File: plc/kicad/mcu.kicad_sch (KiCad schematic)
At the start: 66 parts, among them J1 Conn_01x03_Pin, J2 Conn_01x04_Pin, Q3 L8050QLT1G, Q4 L8050QLT1G, SW1 TSD003B08026A03, SW2 TSD003B08026A03, U10 ESP32-S3-MINI-1U, U11 BS-0601-SK-4W, U12 AHT20_C2757850, U13 CP2102N-A02-GQFN28R, U9 RV-3028-C7

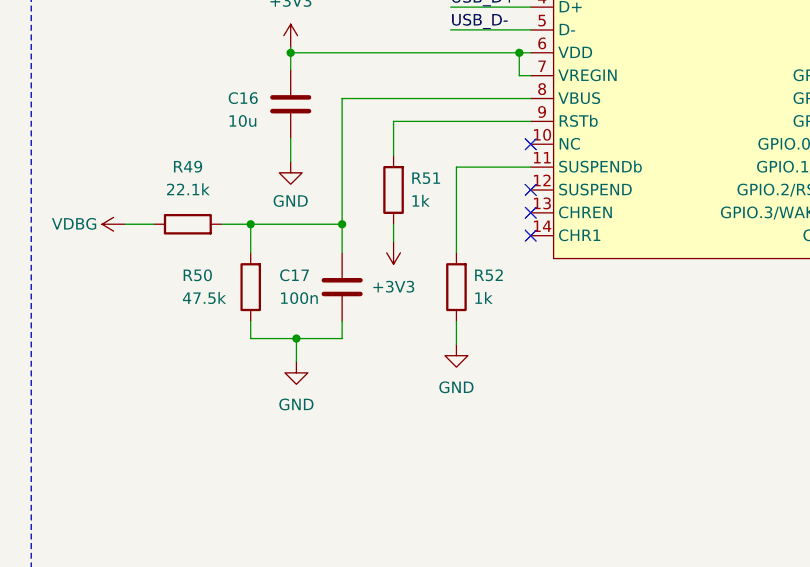
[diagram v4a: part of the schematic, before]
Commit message: PCB placement of USB circuits
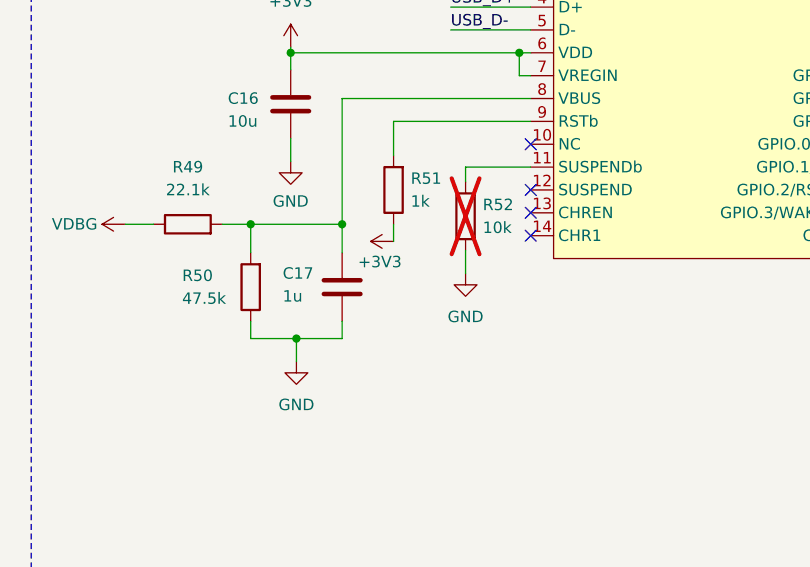
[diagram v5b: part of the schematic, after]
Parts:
- C17: value 100n -> 1u
- R52: value 1k -> 10k; now not fitted; now left out of the parts list
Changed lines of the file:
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@@
 	(wire
 		(pts
-			(xy 278.384 73.914) (xy 270.129 73.914)
+			(xy 278.384 73.914) (xy 271.145 73.914)
 		)
 		(stroke
@@
 	(wire
 		(pts
-			(xy 270.129 93.599) (xy 270.129 91.059)
+			(xy 271.145 85.725) (xy 271.145 83.185)
 		)
 		(stroke
@@
 	(wire
 		(pts
-			(xy 270.129 73.914) (xy 270.129 83.439)
+			(xy 271.145 73.914) (xy 271.145 75.565)
 		)
 		(stroke
@@
 		(dnp no)
 		(property "Reference" "C17"
-			(at 250.444 85.979 0)
+			(at 250.825 85.725 0)
 			(show_name no)
 			(do_not_autoplace no)
@@
 			)
 		)
-		(property "Value" "100n"
-			(at 250.444 88.519 0)
+		(property "Value" "1u"
+			(at 250.825 88.265 0)
 			(show_name no)
 			(do_not_autoplace no)
@@
 	(symbol
 		(lib_id "Device:R")
-		(at 270.129 87.249 180)
+		(at 271.145 79.375 180)
 		(unit 1)
 		(body_style 1)
 		(exclude_from_sim no)
-		(in_bom yes)
-		(on_board yes)
-		(in_pos_files yes)
-		(dnp no)
+		(in_bom no)
+		(on_board no)
+		(in_pos_files no)
+		(dnp yes)
 		(fields_autoplaced yes)
 		(property "Reference" "R52"
-			(at 272.034 85.9789 0)
+			(at 273.05 78.1049 0)
 			(show_name no)
 			(do_not_autoplace no)
@@
 			)
 		)
-		(property "Value" "1k"
-			(at 272.034 88.5189 0)
+		(property "Value" "10k"
+			(at 273.05 80.6449 0)
 			(show_name no)
 			(do_not_autoplace no)
@@
 		)
 		(property "Footprint" "Resistor_SMD:R_0603_1608Metric"
-			(at 271.907 87.249 90)
+			(at 272.923 79.375 90)
 			(hide yes)
 			(show_name no)
@@
 		)
 		(property "Datasheet" ""
-			(at 270.129 87.249 0)
+			(at 271.145 79.375 0)
 			(hide yes)
 			(show_name no)
@@
 		)
 		(property "Description" "Resistor"
-			(at 270.129 87.249 0)
+			(at 271.145 79.375 0)
 			(hide yes)
 			(show_name no)
@@
 	(symbol
 		(lib_id "power:GND")
-		(at 270.129 93.599 0)
+		(at 271.145 85.725 0)
 		(unit 1)
 		(body_style 1)
@@
 		(fields_autoplaced yes)
 		(property "Reference" "#PWR0109"
-			(at 270.129 99.949 0)
+			(at 271.145 92.075 0)
 			(hide yes)
 			(show_name no)
@@
 		)
 		(property "Value" "GND"
-			(at 270.129 98.425 0)
+			(at 271.145 90.551 0)
 			(show_name no)
 			(do_not_autoplace no)
@@
 		)
 		(property "Footprint" ""
-			(at 270.129 93.599 0)
+			(at 271.145 85.725 0)
 			(hide yes)
 			(show_name no)
@@
 		)
 		(property "Datasheet" ""
-			(at 270.129 93.599 0)
+			(at 271.145 85.725 0)
 			(hide yes)
 			(show_name no)
@@
 		)
 		(property "Description" "Power symbol creates a global label with name \"GND\" , ground"
-			(at 270.129 93.599 0)
+			(at 271.145 85.725 0)
 			(hide yes)
 			(show_name no)
@@
 	(symbol
 		(lib_id "power:+3V3")
-		(at 263.144 82.169 180)
+		(at 263.144 82.169 90)
 		(unit 1)
 		(body_style 1)
@@
 		(in_pos_files yes)
 		(dnp no)
-		(fields_autoplaced yes)
 		(property "Reference" "#PWR0107"
-			(at 263.144 78.359 0)
+			(at 266.954 82.169 0)
 			(hide yes)
 			(show_name no)
@@
 		)
 		(property "Value" "+3V3"
-			(at 263.144 87.249 0)
+			(at 261.62 84.455 90)
 			(show_name no)
 			(do_not_autoplace no)

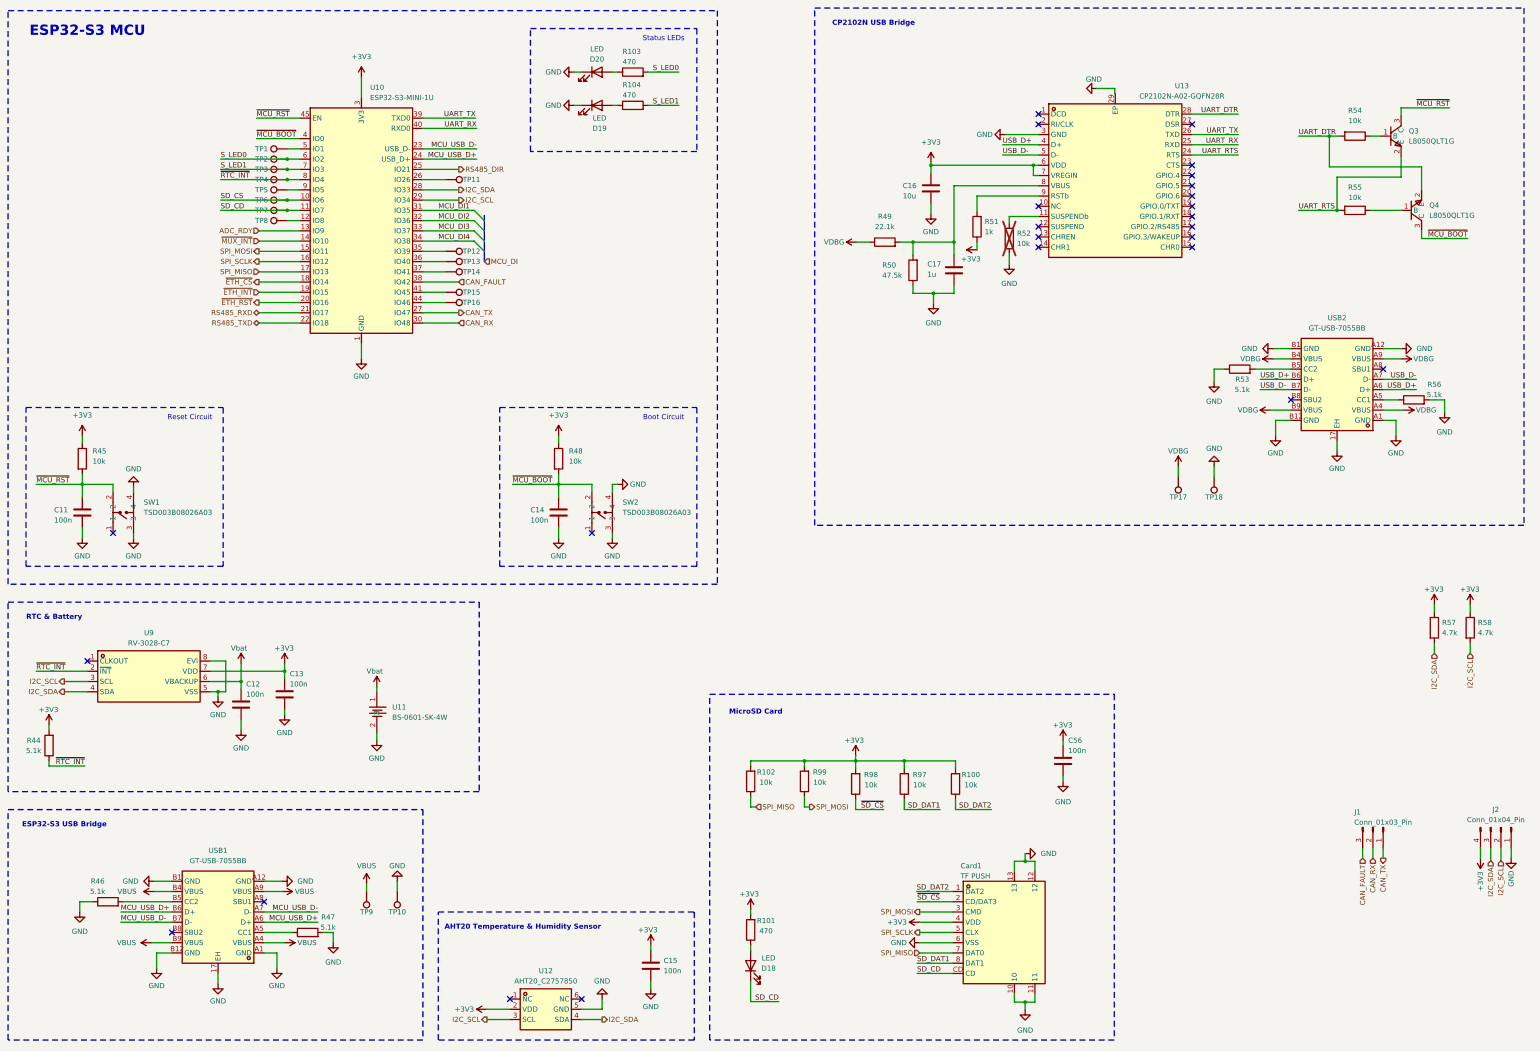
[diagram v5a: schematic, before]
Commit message: Rearranged small PCB placements
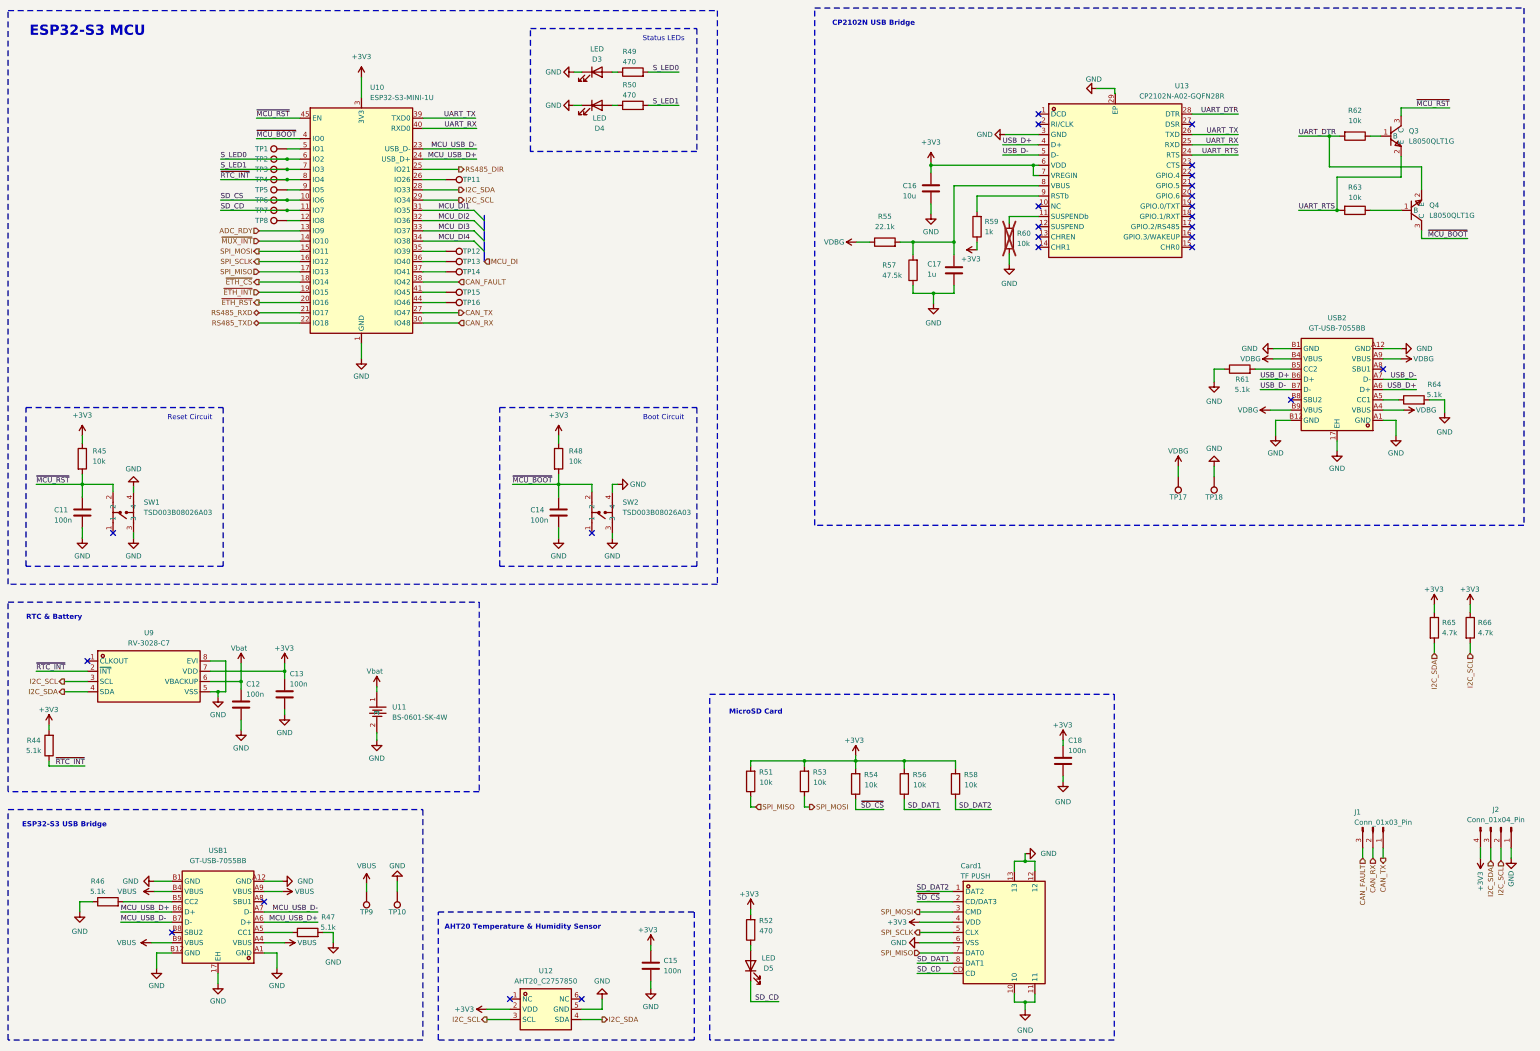
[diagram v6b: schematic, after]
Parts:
- renumbered C56 to C18, D20 to D3, D19 to D4, D18 to D5, R103 to R49, R104 to R50, R102 to R51, R101 to R52, R99 to R53, R98 to R54, R49 to R55, R97 to R56, R50 to R57, R100 to R58, R51 to R59, R52 to R60, R53 to R61, R54 to R62, R55 to R63, R56 to R64, R57 to R65, R58 to R66

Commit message: PCB placement updates
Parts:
- U10: footprint RF_Module:ESP32-S2-MINI-1U -> LibrePLC32:BULETM-SMD_ESPRESSIF_ESP32-S3-MINI-1U-N8
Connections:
- net ~{MCU_RST}: no longer U10.45 (EN)
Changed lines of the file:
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@@
 	(wire
 		(pts
-			(xy 134.62 97.79) (xy 125.73 97.79)
+			(xy 125.73 52.07) (xy 139.065 52.07)
 		)
 		(stroke
@@
 	(wire
 		(pts
-			(xy 84.455 49.53) (xy 95.25 49.53)
+			(xy 134.62 97.79) (xy 125.73 97.79)
 		)
 		(stroke
@@
 	(wire
 		(pts
-			(xy 125.73 49.53) (xy 138.811 49.53)
-		)
-		(stroke
-			(width 0)
-			(type default)
-		)
-	)
-	(wire
-		(pts
 			(xy 59.69 260.35) (xy 59.69 256.54)
 		)
@@
 	(wire
 		(pts
+			(xy 139.065 59.69) (xy 125.73 59.69)
+		)
+		(stroke
+			(width 0)
+			(type default)
+		)
+	)
+	(wire
+		(pts
+			(xy 139.065 57.15) (xy 125.73 57.15)
+		)
+		(stroke
+			(width 0)
+			(type default)
+		)
+	)
+	(wire
+		(pts
 			(xy 248.285 259.08) (xy 257.175 259.08)
 		)
@@
 	(wire
 		(pts
-			(xy 125.73 59.69) (xy 139.065 59.69)
-		)
-		(stroke
-			(width 0)
-			(type default)
-		)
-	)
-	(wire
-		(pts
 			(xy 29.845 186.69) (xy 42.545 186.69)
 		)
@@
 	(wire
 		(pts
-			(xy 125.73 52.07) (xy 139.065 52.07)
-		)
-		(stroke
-			(width 0)
-			(type default)
-		)
-	)
-	(wire
-		(pts
 			(xy 278.384 61.214) (xy 277.114 61.214)
 		)
@@
 	(wire
 		(pts
+			(xy 125.73 49.53) (xy 138.811 49.53)
+		)
+		(stroke
+			(width 0)
+			(type default)
+		)
+	)
+	(wire
+		(pts
 			(xy 131.445 64.77) (xy 125.73 64.77)
 		)
@@
 	(wire
 		(pts
-			(xy 125.73 57.15) (xy 139.065 57.15)
-		)
-		(stroke
-			(width 0)
-			(type default)
-		)
-	)
-	(wire
-		(pts
 			(xy 372.11 116.84) (xy 363.855 116.84)
 		)
@@
 		)
 	)
+	(label "MCU_USB_D+"
+		(at 139.065 59.69 180)
+		(effects
+			(font
+				(size 1.27 1.27)
+			)
+			(justify right bottom)
+		)
+	)
 	(label "S_LED0"
 		(at 189.23 38.1 180)
@@
 		)
 	)
-	(label "UART_RX"
-		(at 139.065 52.07 180)
-		(effects
-			(font
-				(size 1.27 1.27)
-			)
-			(justify right bottom)
-		)
-	)
 	(label "USB_D+"
 		(at 372.11 116.84 180)
@@
 		)
 	)
-	(label "UART_TX"
-		(at 138.811 49.53 180)
-		(effects
-			(font
-				(size 1.27 1.27)
-			)
-			(justify right bottom)
-		)
-	)
 	(label "UART_DTR"
 		(at 342.9 53.975 0)
@@
 		)
 	)
-	(label "~{MCU_RST}"
-		(at 29.845 140.335 0)
+	(label "MCU_USB_D-"
+		(at 139.065 57.15 180)
 		(effects
 			(font
 				(size 1.27 1.27)
 			)
-			(justify left bottom)
+			(justify right bottom)
 		)
 	)
-	(label "UART_RX"
-		(at 327.914 56.134 180)
+	(label "~{MCU_RST}"
+		(at 29.845 140.335 0)
 		(effects
 			(font
 				(size 1.27 1.27)
 			)
-			(justify right bottom)
+			(justify left bottom)
 		)
 	)
-	(label "MCU_USB_D+"
-		(at 139.065 59.69 180)
+	(label "UART_RX"
+		(at 327.914 56.134 180)
 		(effects
 			(font
@@
 		)
 	)
-	(label "~{MCU_RST}"
-		(at 84.455 49.53 0)
+	(label "UART_DTR"
+		(at 327.914 48.514 180)
 		(effects
 			(font
 				(size 1.27 1.27)
 			)
-			(justify left bottom)
+			(justify right bottom)
 		)
 	)
-	(label "UART_DTR"
-		(at 327.914 48.514 180)
+	(label "UART_RX"
+		(at 139.065 52.07 180)
 		(effects
 			(font
@@
 		)
 	)
-	(label "MCU_USB_D-"
-		(at 99.695 246.38 180)
+	(label "UART_TX"
+		(at 138.811 49.53 180)
 		(effects
 			(font
@@
 	)
 	(label "MCU_USB_D-"
-		(at 139.065 57.15 180)
+		(at 99.695 246.38 180)
 		(effects
 			(font
@@
 			)
 		)
-		(property "Footprint" "RF_Module:ESP32-S2-MINI-1U"
+		(property "Footprint" "LibrePLC32:BULETM-SMD_ESPRESSIF_ESP32-S3-MINI-1U-N8"
 			(at 127 104.14 0)
 			(hide yes)

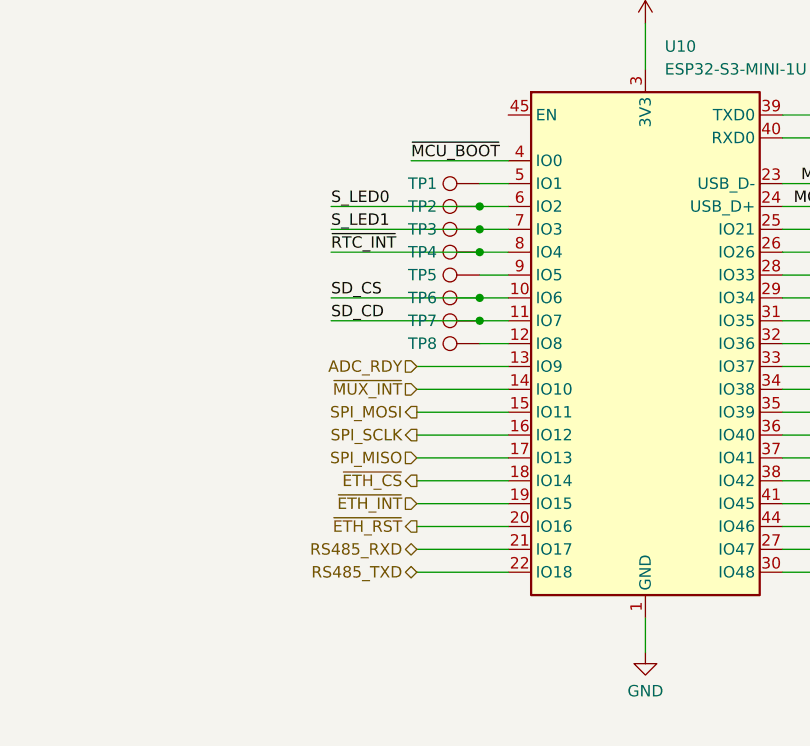
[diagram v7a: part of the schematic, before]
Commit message: Updated PCB placement
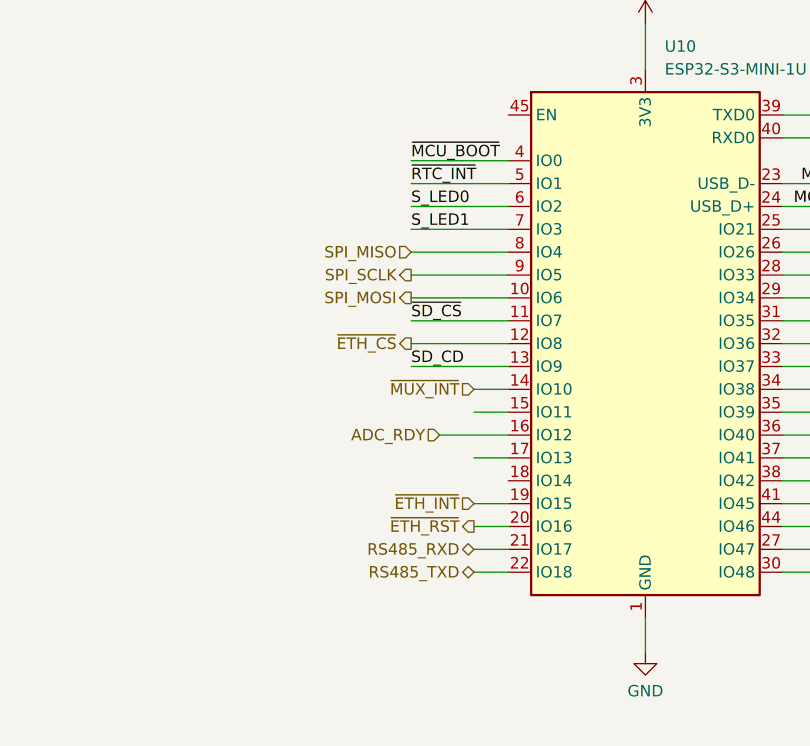
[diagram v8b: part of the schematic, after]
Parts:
- removed TP1, TP2, TP3, TP4, TP5, TP6, TP7, TP8: TestPoint, TestPoint:TestPoint_Pad_D2.0mm, symbol Connector:TestPoint
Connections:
- net SD_CS is gone; now on net SPI_MOSI: U10.10 (IO6)
- net ADC_RDY: now also U10.16 (IO12); no longer U10.13 (IO9)
- net SD_CD: now also U10.13 (IO9); no longer U10.11 (IO7)
- net SPI_MISO: now also U10.8 (IO4); no longer U10.17 (IO13)
- net SPI_MOSI: no longer U10.15 (IO11)
- net SPI_SCLK: now also U10.9 (IO5); no longer U10.16 (IO12)
- net ~{ETH_CS}: now also U10.12 (IO8); no longer U10.18 (IO14)
- net ~{RTC_INT}: now also U10.5 (IO1); no longer U10.8 (IO4)
- net ~{SD_CS}: now also U10.11 (IO7)
